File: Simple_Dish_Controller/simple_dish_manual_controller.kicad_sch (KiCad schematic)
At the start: 12 parts, among them J1 Screw_Terminal_01x02, J2 Conn_01x02_Pin, J3 Screw Terminal To Chassis, U1 AMS1117-5.0, U2 74LS32, U3 74LS08

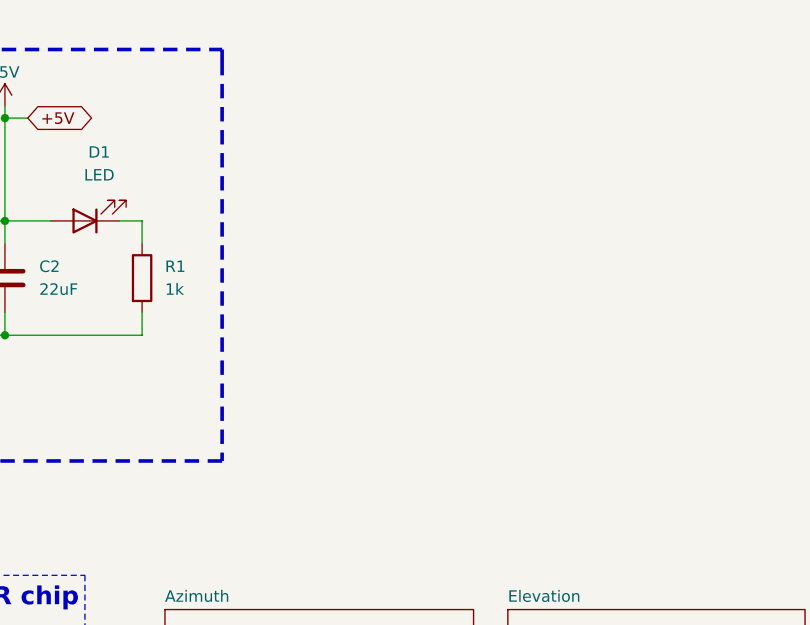
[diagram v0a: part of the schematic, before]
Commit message: PCB outline defined, origin and drill holes established, hole positioning completed. Beginning component placement.
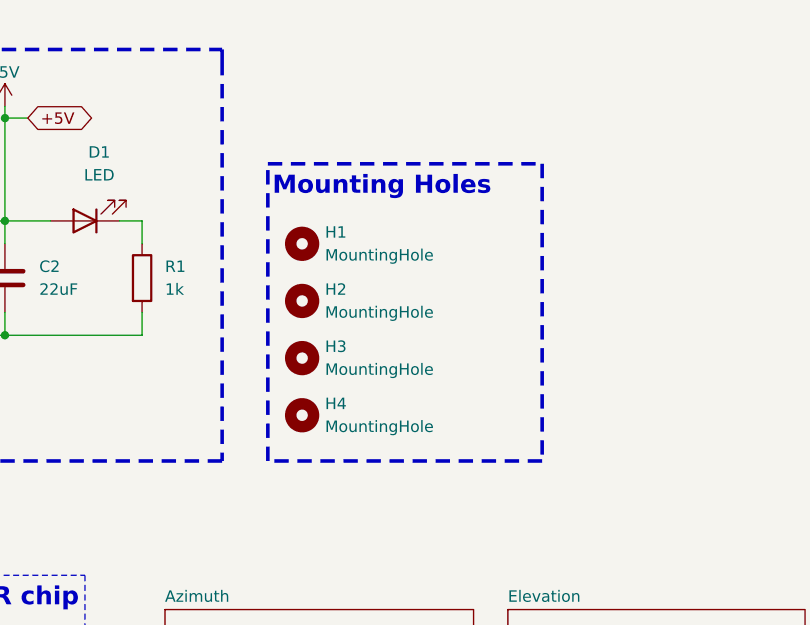
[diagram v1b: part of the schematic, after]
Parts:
- added H1, H2, H3, H4: MountingHole, MountingHole:MountingHole_2.7mm_M2.5, symbol Mechanical:MountingHole
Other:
- note added: "Mounting Holes"

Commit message: Final version of the PCB.Production files were generated in -Production- folder
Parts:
- C1, C2: LCSC Part (none) -> C12891
- C3, C4: value 0.1uF -> 100nF; LCSC Part (none) -> C24497
- D1: LCSC Part (none) -> C5264252
- R1: footprint Resistor_SMD:R_0805_2012Metric -> Resistor_SMD:R_1206_3216Metric; LCSC Part (none) -> C4410
- U1: LCSC Part (none) -> C6187
- U2: LCSC Part (none) -> C116812
- U3: LCSC Part (none) -> C6802
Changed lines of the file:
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@@
 			"AAAAAAAAAAAAAAAAAAAAAAAAAAAAAAAAAAAAAAAAAAAAAAAAAAAAAAAAAAAAAAAAAAAAAAAAAAAA"
 			"AAAAAAAAAAAAAAAAAAAAAAAAAAAAAAAAAAAAAAAAAAAAAAAAAAAAAAAAAAAAAAAAAAAAAAAAAAAA"
-			"AAAAAAAAAAAAAAAAAAAAAAAAAAAAAAAAAAAAAA=="
+			"AAAAAAAAAAAAAAAAAAAAAAAAAAAAAAAAAAAAAADEJQAAAAAAAHw1NgwAAAAAqVElBQAAAADFJQAA"
+			"AAAAAO1gNwwAAAAAzREnBQAAAADGJQAAAAAAAPBgNwwAAAAA0REnBQAAAADHJQAAAAAAAA7eOAwA"
+			"AAAA744oBQAAAADIJQAAAAAAABLeOAwAAAAA8o4oBQAAAADJJQAAAAAAADaeOgwAAAAAY7opBQAA"
+			"AADKJQAAAAAAAEOeOgwAAAAAaropBQAAAADLJQAAAAAAADOQPAwAAAAAqogqBQAAAADMJQAAAAAA"
+			"ADiQPAwAAAAArIgqBQAAAADNJQAAAAAAADyQPAwAAAAArIgqBQAAAADOJQAAAAAAAD2QPAwAAAAA"
+			"rYgqBQAAAADPJQAAAAAAANygPgwAAAAA1PEqBQAAAADQJQAAAAAAAN+gPgwAAAAA1PEqBQAAAADR"
+			"JQAAAAAAAOO7QAwAAAAA1PEqBQAAAADSJQAAAAAAAIkfQgwAAAAAFasqBQAAAADTJQAAAAAAAIjM"
+			"QgwAAAAArIgqBQAAAADUJQAAAAAAAIO+RAwAAAAAZ7opBQAAAADVJQAAAAAAAK5+RgwAAAAA8o4o"
+			"BQAAAADWJQAAAAAAANL7RwwAAAAAzhEnBQAAAADXJQAAAAAAAEcnSQwAAAAAo1ElBQAAAADYJQAA"
+			"AAAAAIz1SQwAAAAAqF8jBQAAAADZJQAAAAAAAMEYSgwAAAAAqa4iBQAAAADaJQAAAAAAALReSgwA"
+			"AAAAA08hBQAAAADbJQAAAAAAALReSgwAAAAA/DMfBQAAAADcJQAAAAAAAI31SQwAAAAAXSMdBQAA"
+			"AADdJQAAAAAAAIz1SQwAAAAAXCMdBQAAAADeJQAAAAAAAIz1SQwAAAAAWCMdBQAAAADfJQAAAAAA"
+			"AI7XSQwAAAAA8NocBQAAAADgJQAAAAAAAEonSQwAAAAAYzEbBQAAAADhJQAAAAAAAEMnSQwAAAAA"
+			"VjEbBQAAAADiJQAAAAAAANL7RwwAAAAAMnEZBQAAAADjJQAAAAAAAM/7RwwAAAAALnEZBQAAAADk"
+			"JQAAAAAAALF+RgwAAAAAEPQXBQAAAADlJQAAAAAAAK1+RgwAAAAADfQXBQAAAADmJQAAAAAAAIm+"
+			"RAwAAAAAnMgWBQAAAADnJQAAAAAAAHy+RAwAAAAAlcgWBQAAAADoJQAAAAAAAIzMQgwAAAAAVfoV"
+			"BQAAAADpJQAAAAAAAILMQgwAAAAAUvoVBQAAAADqJQAAAAAAAOO7QAwAAAAALJEVBQAAAADrJQAA"
+			"AAAAAOG7QAwAAAAALJEVBQAAAADsJQAAAAAAAN+gPgwAAAAALJEVBQAAAADtJQAAAAAAAN2gPgwA"
+			"AAAALJEVBQAAAADuJQAAAAAAAD2QPAwAAAAAUg=="
 		)
 	)
@@
 			)
 		)
-		(property "LCSC Part" ""
+		(property "LCSC Part" "C116812"
 			(at 175.26 135.89 0)
 			(effects
@@
 					(size 1.27 1.27)
 				)
+				(hide yes)
 			)
 		)
@@
 			)
 		)
-		(property "LCSC Part" ""
+		(property "LCSC Part" "C12891"
 			(at 162.56 87.63 0)
 			(effects
@@
 					(size 1.27 1.27)
 				)
+				(hide yes)
 			)
 		)
@@
 			)
 		)
-		(property "LCSC Part" ""
+		(property "LCSC Part" "C116812"
 			(at 86.36 149.86 0)
 			(effects
@@
 					(size 1.27 1.27)
 				)
+				(hide yes)
 			)
 		)
@@
 			)
 		)
-		(property "LCSC Part" ""
+		(property "LCSC Part" "C12891"
 			(at 187.96 87.63 0)
 			(effects
@@
 					(size 1.27 1.27)
 				)
+				(hide yes)
 			)
 		)
@@
 			)
 		)
-		(property "Value" "0.1uF"
+		(property "Value" "100nF"
 			(at 80.01 137.1599 0)
 			(effects
@@
 			)
 		)
-		(property "LCSC Part" ""
+		(property "LCSC Part" "C24497"
 			(at 76.2 135.89 0)
 			(effects
@@
 					(size 1.27 1.27)
 				)
+				(hide yes)
 			)
 		)
@@
 			)
 		)
-		(property "LCSC Part" ""
+		(property "LCSC Part" "C116812"
 			(at 175.26 149.86 0)
 			(effects
@@
 					(size 1.27 1.27)
 				)
+				(hide yes)
 			)
 		)
@@
 			)
 		)
-		(property "Footprint" "Resistor_SMD:R_0805_2012Metric"
+		(property "Footprint" "Resistor_SMD:R_1206_3216Metric"
 			(at 201.422 87.63 90)
 			(effects
@@
 			)
 		)
-		(property "LCSC Part" ""
+		(property "LCSC Part" "C4410"
 			(at 203.2 87.63 0)
 			(effects
@@
 					(size 1.27 1.27)
 				)
+				(hide yes)
 			)
 		)
@@
 			)
 		)
-		(property "LCSC Part" ""
+		(property "LCSC Part" "C5264252"
 			(at 196.85 81.28 0)
 			(effects
@@
 					(size 1.27 1.27)
 				)
+				(hide yes)
 			)
 		)
@@
 			)
 		)
-		(property "LCSC Part" ""
+		(property "LCSC Part" "C6187"
 			(at 175.26 81.28 0)
 			(effects
@@
 					(size 1.27 1.27)
 				)
+				(hide yes)
 			)
 		)
@@
 			)
 		)
-		(property "Value" "0.1uF"
+		(property "Value" "100nF"
 			(at 58.42 137.1599 0)
 			(effects
@@
 			)
 		)
-		(property "LCSC Part" ""
+		(property "LCSC Part" "C24497"
 			(at 54.61 135.89 0)
 			(effects
@@
 					(size 1.27 1.27)
 				)
+				(hide yes)
 			)
 		)
@@
 			)
 		)
-		(property "LCSC Part" ""
+		(property "LCSC Part" "C6802"
 			(at 64.77 149.86 0)
 			(effects
@@
 					(size 1.27 1.27)
 				)
+				(hide yes)
 			)
 		)
